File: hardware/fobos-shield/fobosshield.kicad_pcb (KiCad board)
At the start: 4 copper layers, 76.5 x 68.6 mm, 166 parts, among them J1 Target, J10 ADCin, J11 PP1, J12 PP2, J13 Clock, J14 Trigger, J15 CSM5VCur, J16 Conn_01x01, J17 Barrel_Jack_Switch, J18 Conn_01x02, J19 Conn_01x02, J2 Glitch, J20 CSM3V3Cur, J21 GND, J22 GND, J23 CSM5VCur, J24 Conn_01x02, J25 V_Var, J3 Analog, J4 IOH, J5 SPI, J6 Analog2, J7 Power, J8 IOL, J9 SPI2, Q1 IRF7807Z, Q2 IRLML2502, Q3 BSS138L, Q4 BSS138L, U1 RB-0509D, U10 INA225, U11 INA225, U12 LD1117S33TR_SOT223, U13 INA225, U2 REE-0505S, U3 LM317L_SO8, U4 LM337L_SO8, U5 LD59015, U6 LP3985IM5-3.0, U7 AD8331, U8 TPS7A7100_VQFN20, U9 AD9215

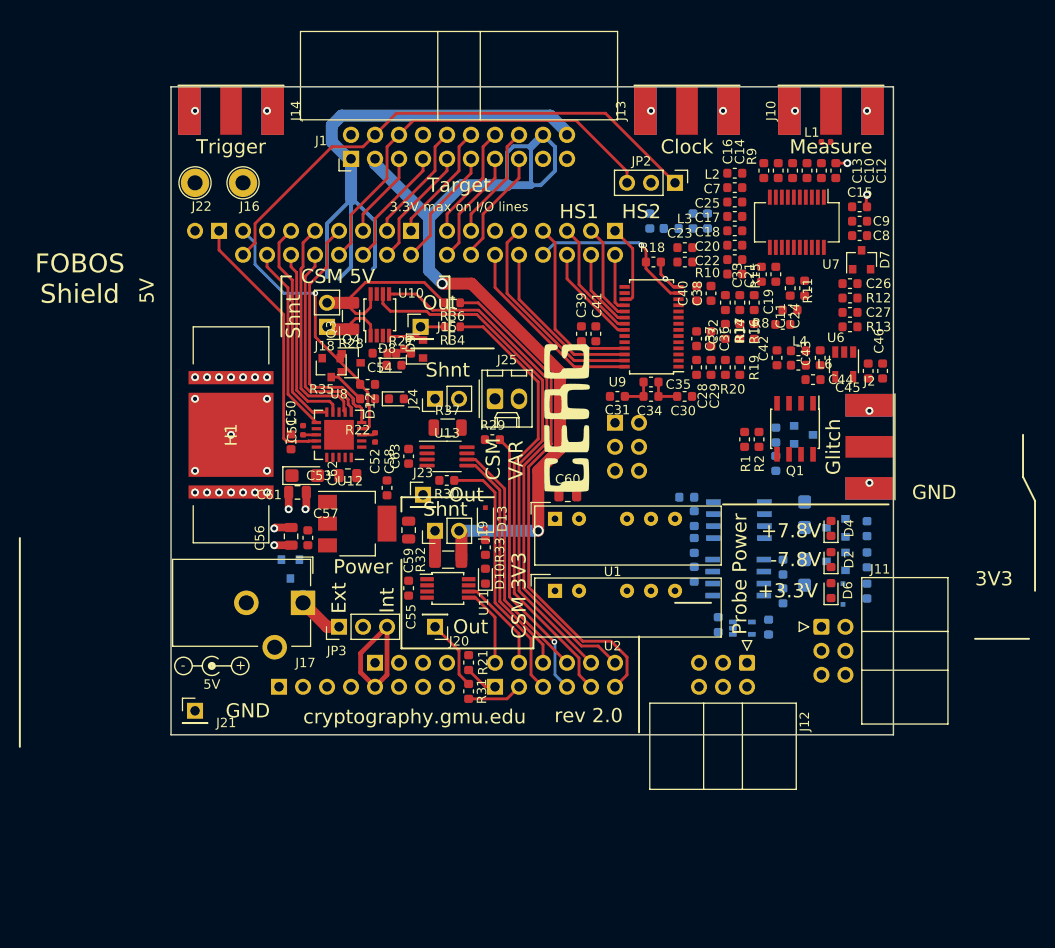
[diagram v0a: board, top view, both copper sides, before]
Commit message: more adjustments on shield PCB part locations
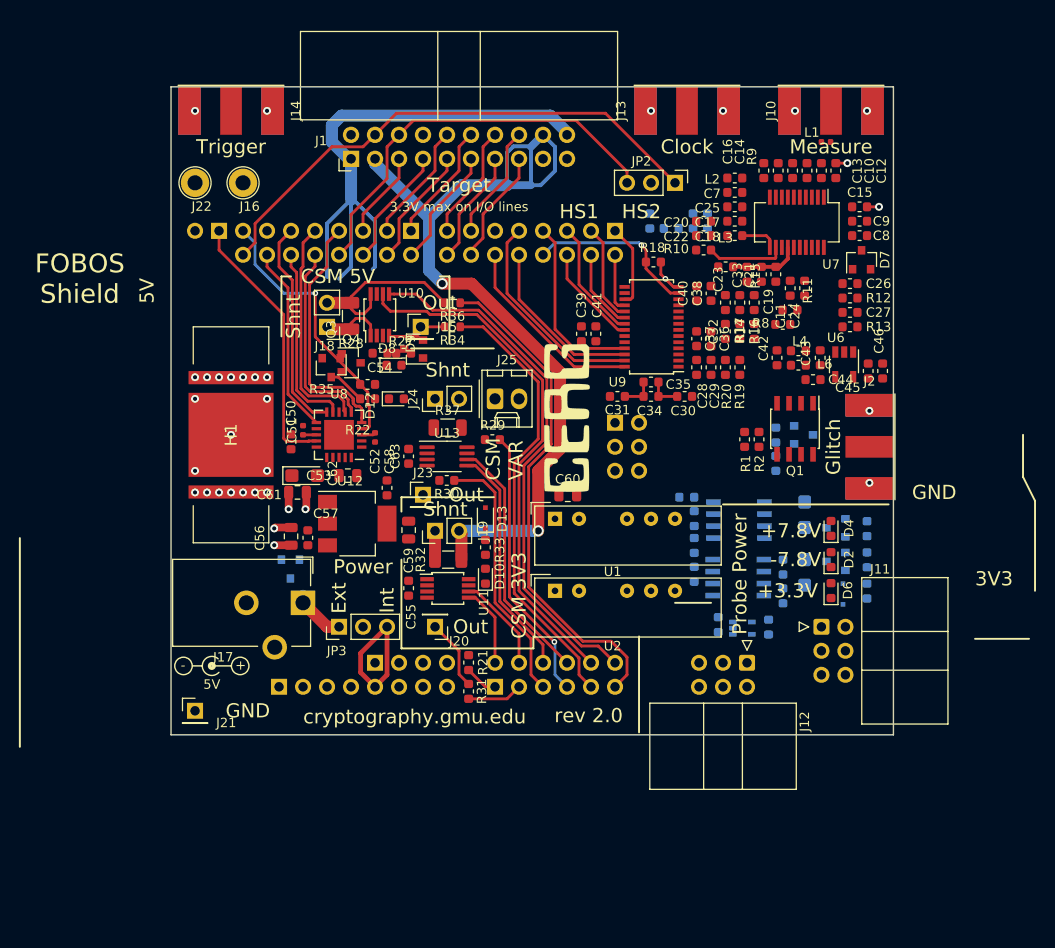
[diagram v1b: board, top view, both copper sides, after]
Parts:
- J17: footprint Connector_BarrelJack:BarrelJack_CUI_PJ-102AH_Horizontal -> cerg:BarrelJack_CUI_PJ-102AH_Horizontal
- moved C23 6.70 mm to (97.8, 35.1), turned to 90 degrees
- moved L3 4.77 mm to (95.5, 34.3)
- moved C20 4.17 mm to (93.2, 29.5)
- moved C22 4.17 mm to (93.2, 31.0)
- moved R10 4.17 mm to (93.2, 32.5)
- moved C25 0.51 mm to (96.5, 27.9)
- moved C17 0.51 mm to (96.5, 29.5)
- moved C18 0.51 mm to (96.5, 31.0)
- moved C7 0.51 mm to (96.5, 26.4)
- moved L2 0.51 mm to (96.5, 24.9)
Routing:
- net Net-(C20-Pad2): track 0.00 -> 8.36 mm
- net Net-(C19-Pad2): track 0.00 -> 7.35 mm
- net Net-(C17-Pad2): track 0.00 -> 3.94 mm

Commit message: tiny changes on FOBOS2 shield
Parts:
- moved J22 10.2 mm to (40.6, 35.6)
- moved C8 5.04 mm to (111.3, 26.2), turned to 270 degrees
- moved C20 4.83 mm to (97.3, 32.0), turned to 270 degrees
- moved C15 4.18 mm to (108.7, 23.9)
- moved JP2 3.81 mm to (90.2, 21.6)
- moved C9 3.28 mm to (109.7, 26.2), turned to 270 degrees
- moved J16 2.84 mm to (43.2, 22.9)
- moved C22 2.77 mm to (95.8, 32.0), turned to 270 degrees
- moved C10 2.74 mm to (106.7, 21.6)
- moved C13 2.74 mm to (105.2, 21.6)
- moved R9 2.74 mm to (103.6, 21.6)
- moved C12 2.74 mm to (108.2, 21.6)
- moved C31 2.58 mm to (86.6, 48.3)
- moved J10 2.54 mm to (106.7, 15.2)
- moved J13 2.54 mm to (91.4, 15.2)
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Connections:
- J5 pad 1: VGA_GAIN -> VGA_HILO
- J5 pad 3: VGA_HILO -> VGA_GAIN
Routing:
- net GNDA: track 2.82 -> 58.1 mm, vias 4 -> 18
- net ADC_OR: track 0.00 -> 34.4 mm, vias 0 -> 2
- net Net-(C25-Pad2): track 0.00 -> 31.1 mm
- net Trigger: track 0.00 -> 16.8 mm
- net Net-(C26-Pad2): track 0.00 -> 15.7 mm, vias 0 -> 2
- net 5Vclean: track 0.00 -> 14.0 mm, vias 0 -> 2
- net VGA_HILO: track 0.00 -> 10.8 mm
- net Net-(J13-Pad1): track 0.00 -> 7.93 mm
- net Net-(R19-Pad1): track 0.00 -> 7.76 mm
- net Net-(C16-Pad2): track 0.00 -> 7.40 mm
- net Net-(C10-Pad1): track 0.00 -> 6.93 mm
- net Net-(C14-Pad2): track 0.00 -> 4.13 mm
- net Net-(C28-Pad2): track 0.00 -> 3.95 mm
- net Net-(J10-Pad1): track 0.00 -> 3.33 mm
- net Net-(C15-Pad2): track 0.00 -> 3.21 mm
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- added copper zone on In2.Cu, net VDDA
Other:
- board size 76.5 x 68.6 mm -> 76.2 x 71.1 mm
- board text added: "C2D"
- board text added: "D2C"
- board text added: "Mea sure"
- board text removed: "HS1"
- board text removed: "HS2"
- board text removed: "Measure"

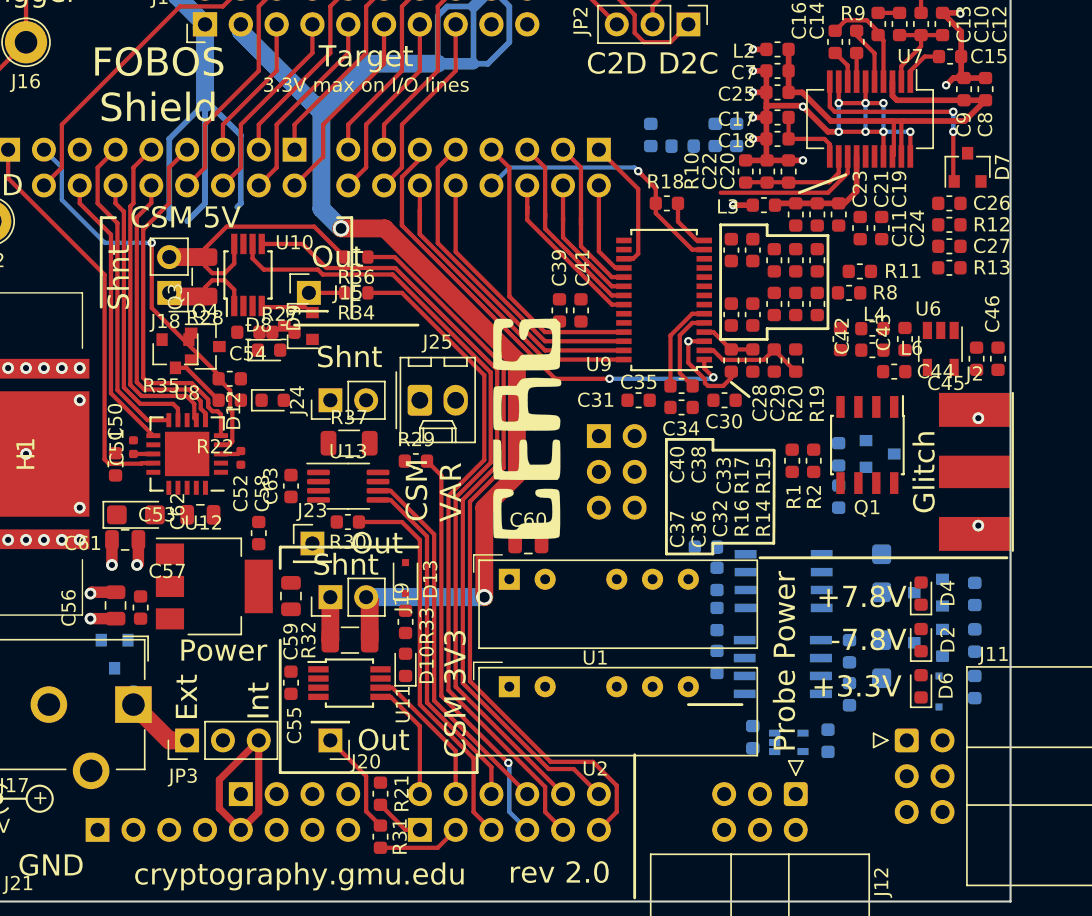
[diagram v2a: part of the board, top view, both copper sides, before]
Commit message: renamed 20-pin connector signals
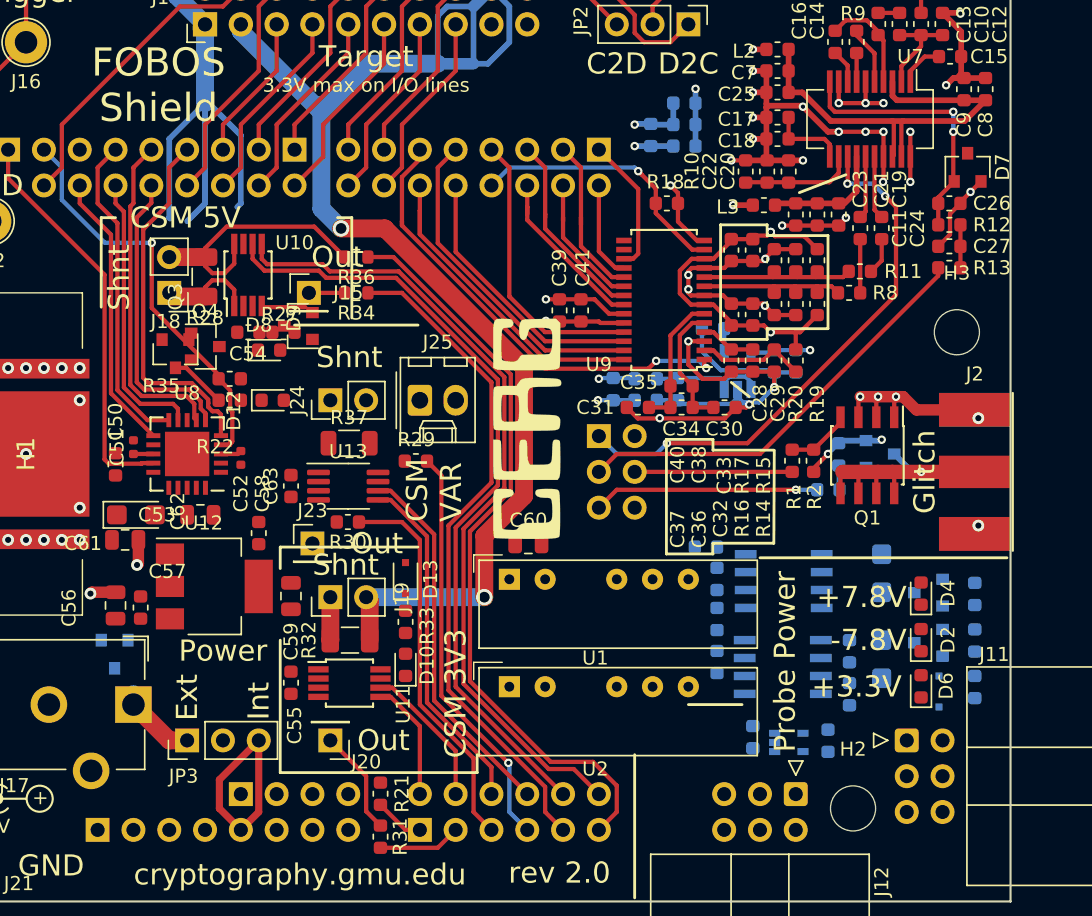
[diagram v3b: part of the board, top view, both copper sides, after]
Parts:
- added H2: MountingHole, MountingHole:MountingHole_3.2mm_M3, F.Cu at (101.9, 77.2)
- added H3: MountingHole, MountingHole:MountingHole_3.2mm_M3, F.Cu at (109.2, 43.4)
- C42, C43, C44, C45, C46, L4, L6, U6: moved to B.Cu
- moved C42 16.5 mm to (84.8, 47.5)
- moved C43 16.5 mm to (89.4, 47.5)
- moved L4 16.5 mm to (87.1, 46.7)
- moved L6 16.5 mm to (87.1, 48.3)
- moved U6 14.5 mm to (93.7, 46.2), turned to 90 degrees
- moved C45 14.4 mm to (96.3, 45.5), turned to 90 degrees
- moved C46 14.4 mm to (97.8, 45.5), turned to 90 degrees
- moved C44 13.2 mm to (91.9, 43.2)
- moved C49 4.34 mm to (89.9, 27.2), turned to 0 degrees
- moved C48 2.31 mm to (89.9, 28.7), turned to 0 degrees
- moved R3 0.88 mm to (100.1, 54.6), turned to 0 degrees
- moved Q1 0.73 mm to (102.9, 52.2)
- moved C31 0.51 mm to (86.6, 48.8)
- moved C30 0.51 mm to (92.7, 48.8)
- moved L5 0.13 mm to (89.9, 30.2)
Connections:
- net CW_HS1 renamed CLK_D2C
- net CW_HS2 renamed CLK_C2D
- net CW_MISO renamed FS_IO
- net CW_MOSI renamed FS_TF
- net CW_PDIC renamed HS_D2C
- net CW_PDID renamed FS_PROG
- net CW_RST renamed FS_RST
- net CW_SCK renamed HS_C2D
- net CW_TARG1 renamed FS_DIO0
- net CW_TARG2 renamed FS_DIO1
- net CW_TARG3 renamed FS_DIO2
- net CW_TARG4 renamed FS_DIO3
- net CW_VREF renamed FS_VREF
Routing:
- net GNDA: track 58.1 -> 132.4 mm, vias 18 -> 31
- net VDDA: track 0.00 -> 40.8 mm, vias 0 -> 4
- net GND: track 7.75 -> 41.1 mm, vias 27 -> 36
- net VGA_GAIN: track 0.00 -> 30.4 mm
- net VGA_HILO: track 10.8 -> 38.6 mm, vias 0 -> 3
- net Net-(J2-Pad1): track 0.00 -> 18.1 mm, vias 0 -> 1
- net GlitchLP: track 0.00 -> 16.0 mm, vias 0 -> 1
- net VCC3V3: track 0.00 -> 13.9 mm, vias 0 -> 2
- net Net-(C33-Pad2): track 0.00 -> 11.3 mm
- net Glitch: track 0.00 -> 11.2 mm
- net Net-(C32-Pad1): track 0.00 -> 11.1 mm
- net Net-(C43-Pad2): track 0.00 -> 8.74 mm
- net 5Vclean: track 14.0 -> 20.6 mm, vias 2 -> 3
- net Net-(Q1-Pad4): track 0.00 -> 4.61 mm
- net Net-(C24-Pad2): track 0.00 -> 4.50 mm
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- removed copper zone on In2.Cu, net IN

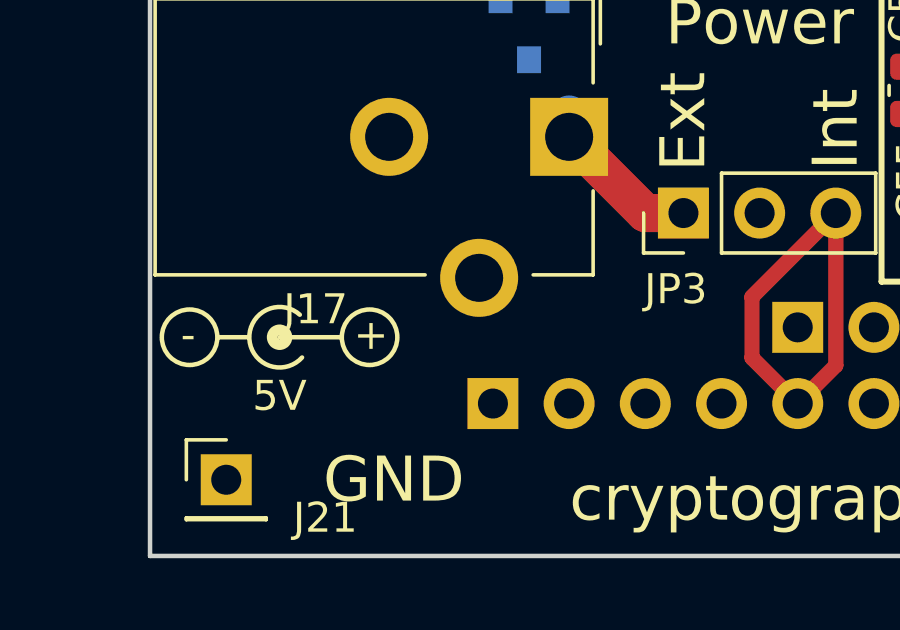
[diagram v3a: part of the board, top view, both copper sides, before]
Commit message: completed change of signal names on target connector
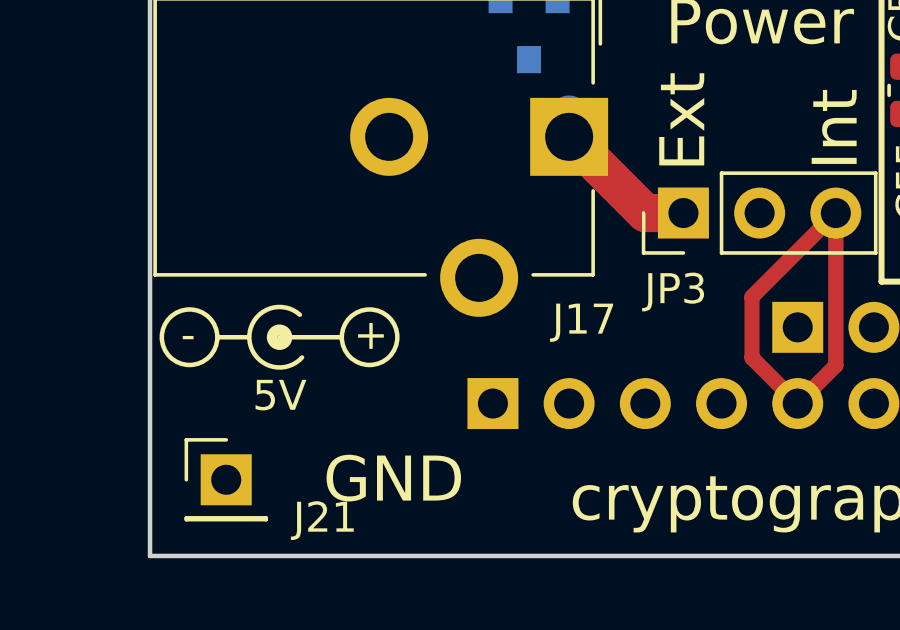
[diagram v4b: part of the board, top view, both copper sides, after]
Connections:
- net CLK_C2D renamed FC2D_CLK
- net CLK_D2C renamed FD2C_CLK
- net CSM3V3 renamed FC_3V3
- net CSM5V renamed FC_5V
- net CSMVar renamed FC_Var
- net FS_DIO0 renamed FC_DIO0
- net FS_DIO1 renamed FC_DIO1
- net FS_DIO2 renamed FC_DIO2
- net FS_DIO3 renamed FC_DIO3
- net FS_IO renamed FC_IO
- net FS_PROG renamed FC_PROG
- net FS_RST renamed FC_RST
- net FS_TF renamed FD_TF
- net FS_VREF renamed FD_VREF
- net HS_C2D renamed FC2D_HS
- net HS_D2C renamed FD2C_HS

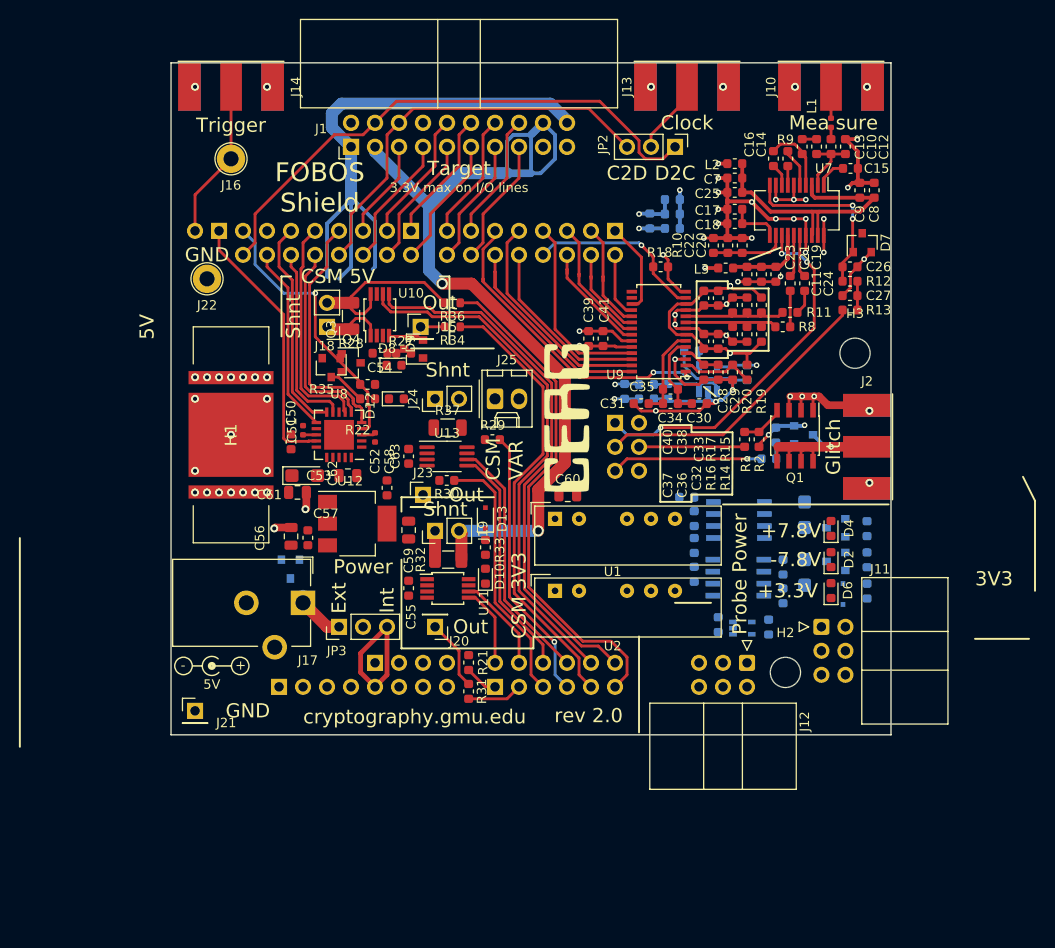
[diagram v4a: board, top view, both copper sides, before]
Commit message: power regulator layout done
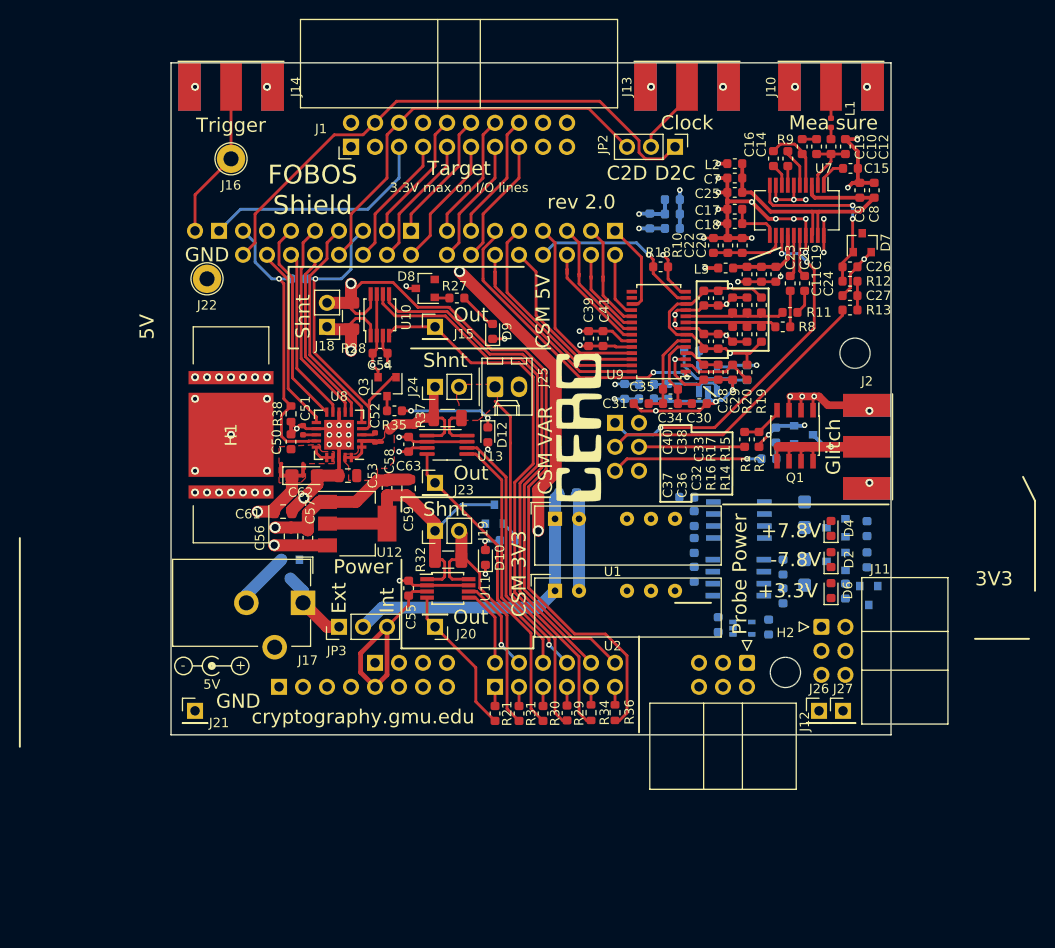
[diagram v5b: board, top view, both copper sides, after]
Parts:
- removed Q4: BSS138L, Package_TO_SOT_SMD:SOT-23
- added J26: AUX, Connector_PinHeader_2.54mm:PinHeader_1x01_P2.54mm_Vertical, F.Cu at (105.4, 81.3)
- added J27: GNDP, Connector_PinHeader_2.54mm:PinHeader_1x01_P2.54mm_Vertical, F.Cu at (108.0, 81.3)
- added R38: 10k, Resistor_SMD:R_0603_1608Metric, F.Cu at (49.5, 49.8)
- C60, R22, R33: moved to B.Cu
- D1: value 5V1 -> 6V3
- D13: value 1N4148 -> 2V1; footprint Diode_SMD:D_SOD-323F -> Diode_SMD:D_SOT-23_ANK; moved to B.Cu
- D3: value 1N4148 -> 2V1; footprint Diode_SMD:D_SOD-323F -> Diode_SMD:D_SOT-23_ANK
- moved R36 46.7 mm to (83.8, 81.5), turned to 270 degrees
- moved R34 43.4 mm to (81.3, 81.5), turned to 270 degrees
- moved R29 30.0 mm to (78.7, 81.5), turned to 270 degrees
- moved R30 26.7 mm to (76.2, 81.6), turned to 270 degrees
- moved R22 13.4 mm to (50.3, 35.6)
- moved D9 11.0 mm to (70.9, 41.1), turned to 90 degrees
- moved D12 10.4 mm to (70.4, 52.1), turned to 270 degrees
- moved R27 8.12 mm to (67.1, 37.6)
- moved D8 6.53 mm to (63.7, 36.6)
- moved Q3 6.24 mm to (59.7, 47.0)
- moved R21 6.07 mm to (71.1, 81.6), turned to 270 degrees
- moved R31 5.82 mm to (73.7, 81.6), turned to 270 degrees
- moved C59 4.41 mm to (62.0, 57.7), turned to 90 degrees
- moved R35 3.12 mm to (60.5, 49.5)
- moved D3 2.73 mm to (110.7, 69.1)
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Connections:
- D13 pad 1: Net-(D13-Pad1) -> Net-(C58-Pad1)
- D13 pad 2: Net-(C58-Pad1) -> Net-(D13-Pad2)
- D3 pad 1: Net-(D3-Pad1) -> /Power/3V3P
- D3 pad 2: /Power/3V3P -> Net-(D3-Pad2)
- J12 pad 3: Net-(J12-Pad3) -> Net-(J11-Pad3)
- J4 pad 15: PWR_PG -> PWR_EN
- J4 pad 5: FC_RST -> PWR_PG
- J9 pad 1: PWR_EN -> FC_RST
- Q3 pad 2: Net-(Q3-Pad2) -> GND
- R21 pad 2: FC_3V3 -> CSM3V3Cur
- R22 pad 1: VCC3V3 -> PWR_PG
- R22 pad 2: PWR_PG -> PWR_EN
- R26 pad 1: Net-(D3-Pad1) -> Net-(D3-Pad2)
- R31 pad 2: CSM3V3Cur -> FC_3V3
- R33 pad 1: Net-(D13-Pad1) -> Net-(D13-Pad2)
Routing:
- net IN: track 6.89 -> 129.3 mm, vias 0 -> 4
- net VCC5V0: track 17.8 -> 94.3 mm, vias 1 -> 3
- net GND: track 41.1 -> 117.1 mm, vias 36 -> 51
- net VCC3V3: track 13.9 -> 84.5 mm, vias 2 -> 3
- net FC_5V: track 81.8 -> 147.2 mm, vias 0 -> 1
- net CSM5VCur: track 5.66 -> 58.9 mm
- net /Ardu/A5: track 53.7 -> 1.91 mm
- net /Ardu/A4: track 47.8 -> 1.91 mm
- net FC_Var: track 0.00 -> 42.2 mm
- net CSMVarCur: track 0.00 -> 33.3 mm
- net Net-(C58-Pad1): track 3.05 -> 31.5 mm
- net /Ardu/A3: track 29.1 -> 1.98 mm, vias 1 -> 0
- net FC_3V3: track 95.1 -> 121.6 mm
- net /Ardu/A2: track 27.5 -> 2.03 mm
- net Net-(C52-Pad1): track 0.00 -> 18.5 mm
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- added copper zone on F.Cu, net FC_Var
- added copper zone on F.Cu, net IN
- added copper zone on F.Cu, net Net-(C52-Pad1)
